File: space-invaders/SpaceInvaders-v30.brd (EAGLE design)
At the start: 127 x 101.6 mm, 26 parts, among them J2-J4 TM4C123GXL, J3-J1 TM4C123GXL, J5 Nokia_5110, J6 Nokia_5110, J7 9V, U1 LM7805CT

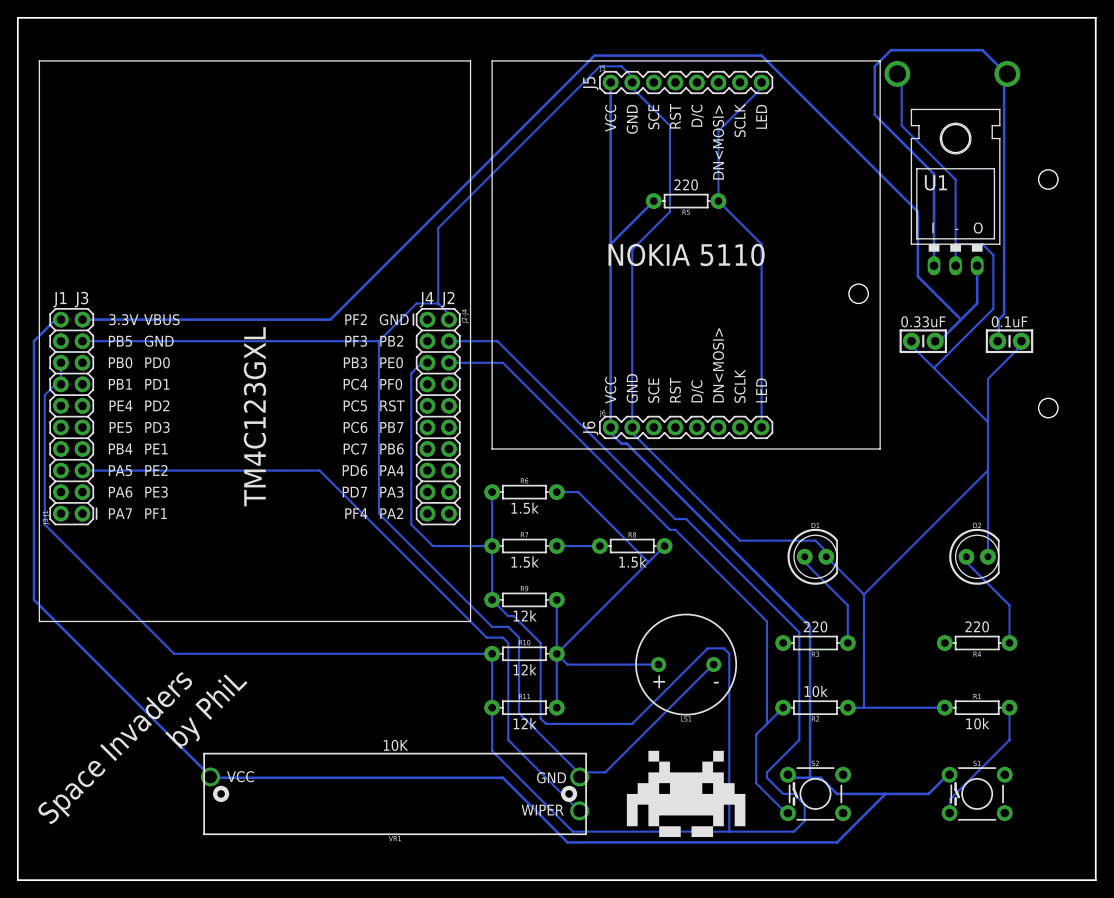
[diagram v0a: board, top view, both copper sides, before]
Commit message: Add versions to file names & Edit stuff
Add versions to file names.
Center Nokia5110 & Edit traces thereof.
Add holes for 9V battery's wires to come through.
v2.1: Replace "SpaceInvaders," "by PhiL," and the sprite icon by Top &
Bottom layers.
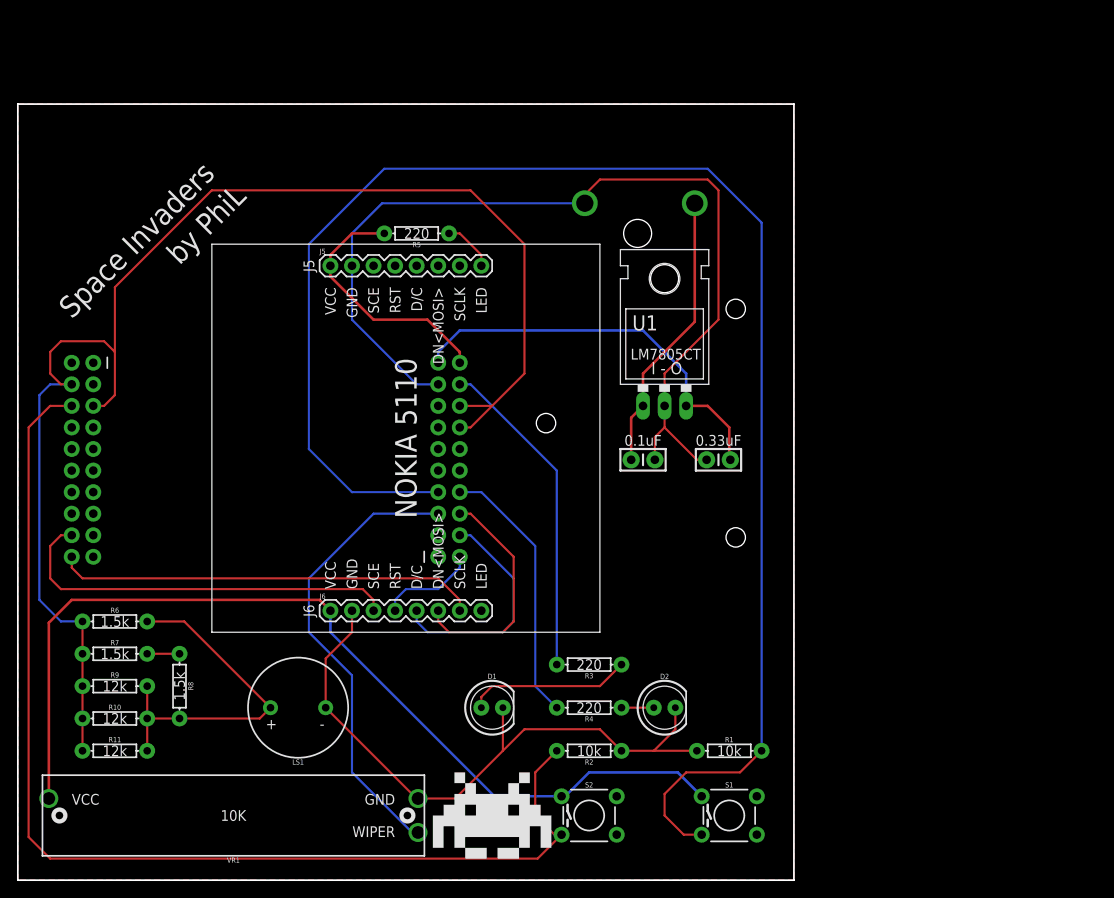
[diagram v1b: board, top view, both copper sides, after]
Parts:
- J5, J6: value Nokia_5110 -> NOKIA_5110
- moved R8 55.8 mm to (19.1, 22.9), turned to 270 degrees
- moved R6 50.6 mm to (11.4, 30.5)
- moved R7 49.9 mm to (11.4, 26.7)
- moved R9 49.3 mm to (11.4, 22.9)
- moved R10 48.9 mm to (11.4, 19.1)
- moved R11 48.5 mm to (11.4, 15.2)
- moved R4 46.4 mm to (67.3, 20.3)
- moved LS1 46.0 mm to (33.0, 20.3)
- moved C2 45.4 mm to (73.7, 49.5)
- moved J3-J1 42.2 mm to (49.5, 38.1), flipped to the bottom
- moved D1 42.0 mm to (55.9, 20.3)
- moved D2 40.9 mm to (76.2, 20.3)
- moved J7 39.9 mm to (58.4, 26.7)
- moved J2-J4 39.7 mm to (8.89, 61.0), flipped to the bottom
- moved J5 39.5 mm to (36.8, 72.4)
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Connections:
- net PB2 renamed DAC
- removed net D/C: J6.5
- removed net DN<MOSI>: J6.6
- removed net RST: J6.4
- removed net SCE: J5.3
- removed net SCLK: J5.7
- net PA2: now also J5.7
- net PA3: now also J5.3
- net PA5: now also J6.6
- net PA6: now also J6.5
- net PA7: now also J6.4
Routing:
- net GND: track 384.2 -> 188.3 mm
- net PE1: track 15.3 -> 184.7 mm
- net DAC: track 321.4 -> 164.8 mm
- net 3.3V: track 269.5 -> 142.3 mm
- net VBUS: track 145.0 -> 47.4 mm
- net PE0: track 77.5 -> 132.1 mm
- net PA2: track 0.00 -> 49.8 mm
- net PA3: track 0.00 -> 47.3 mm
- net 9V: track 76.0 -> 33.3 mm
- net LED: track 44.8 -> 6.13 mm
- net PB5: track 0.00 -> 38.5 mm
- net PB4: track 0.00 -> 31.6 mm
- net PE2: track 81.9 -> 54.1 mm
- net PA6: track 0.00 -> 27.3 mm
- net PA5: track 0.00 -> 27.3 mm
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- added copper zone on layer 1, net GND
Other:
- board size 127 x 101.6 mm -> 91.4 x 91.4 mm
- board text added: "I - O"
- board text added: "LM7805CT"
- board text removed: "I"
- board text removed: "O"
